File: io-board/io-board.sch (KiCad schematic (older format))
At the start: 11 parts, among them J1 EXP, J2 EXP, J3 Conn_01x12, J5 Conn_01x06, U1 W65C22N, U2 74HC138, U3 W65C51N, X1 1.8432MHz

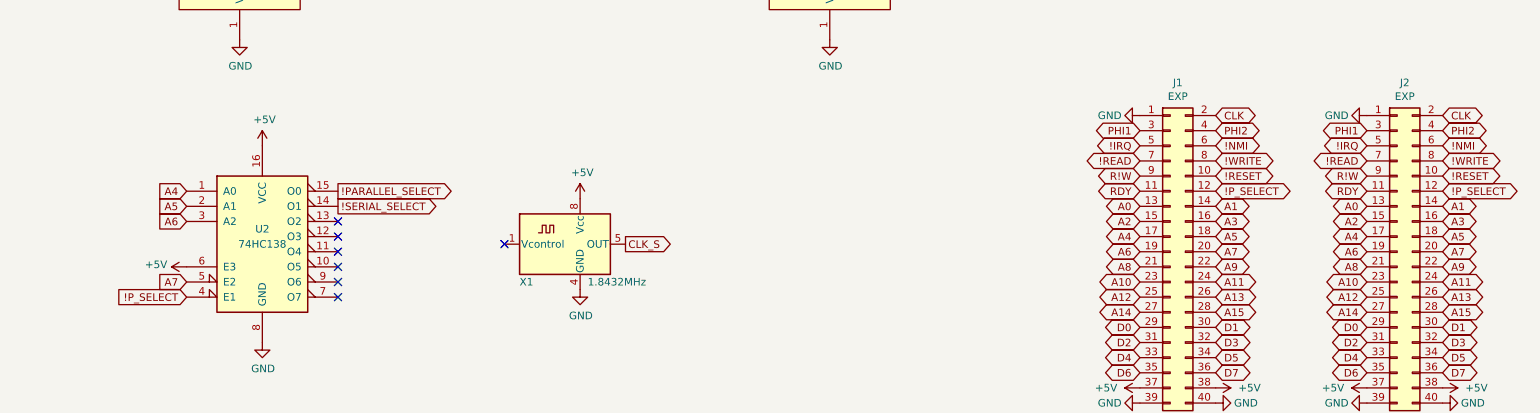
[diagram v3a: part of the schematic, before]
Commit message: remove old peripheral boards, begn new vga design
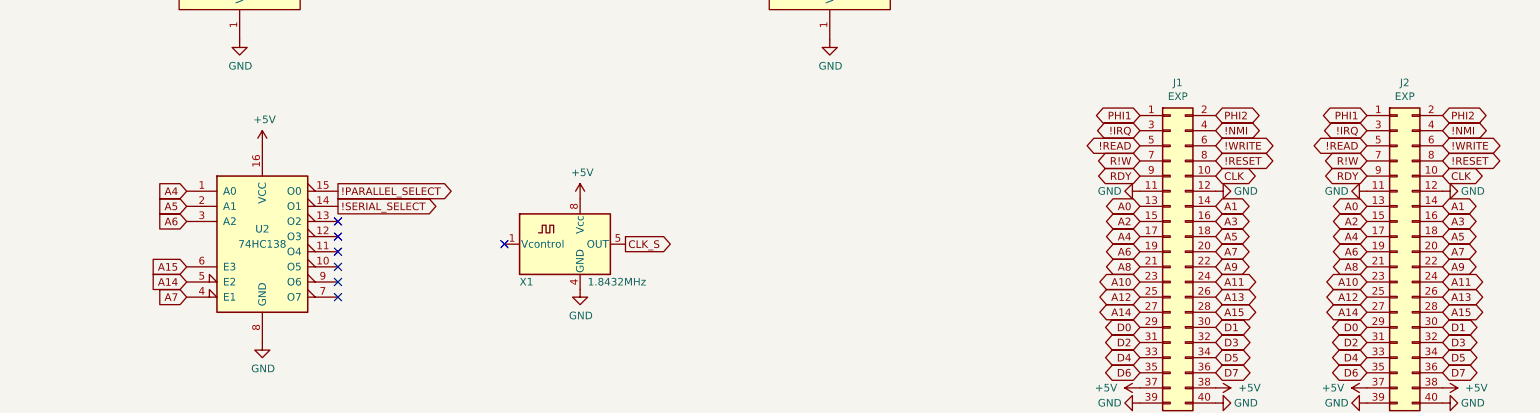
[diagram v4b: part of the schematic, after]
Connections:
- net !IRQ: now also J1.3 (Pin_3), J2.3 (Pin_3); no longer J1.5 (Pin_5), J2.5 (Pin_5)
- net !NMI: now also J1.4 (Pin_4), J2.4 (Pin_4); no longer J1.6 (Pin_6), J2.6 (Pin_6)
- net !READ: now also J1.5 (Pin_5), J2.5 (Pin_5); no longer J1.7 (Pin_7), J2.7 (Pin_7)
- net !RESET: now also J1.8 (Pin_8), J2.8 (Pin_8); no longer J1.10 (Pin_10), J2.10 (Pin_10)
- net !WRITE: now also J1.6 (Pin_6), J2.6 (Pin_6); no longer J1.8 (Pin_8), J2.8 (Pin_8)
- net +5V: no longer U2.6 (E3)
- net A14: now also U2.5 (E2)
- net A15: now also U2.6 (E3)
- net A7: now also U2.4 (E1); no longer U2.5 (E2)
- net CLK: now also J1.10 (Pin_10), J2.10 (Pin_10); no longer J1.2 (Pin_2), J2.2 (Pin_2)
- net GND: now also J1.11 (Pin_11), J1.12 (Pin_12), J2.11 (Pin_11), J2.12 (Pin_12); no longer J1.1 (Pin_1), J2.1 (Pin_1)
- net PHI1: now also J1.1 (Pin_1), J2.1 (Pin_1); no longer J1.3 (Pin_3), J2.3 (Pin_3)
- net PHI2: now also J1.2 (Pin_2), J2.2 (Pin_2); no longer J1.4 (Pin_4), J2.4 (Pin_4)
- net R!W: now also J1.7 (Pin_7), J2.7 (Pin_7); no longer J1.9 (Pin_9), J2.9 (Pin_9)
- net RDY: now also J1.9 (Pin_9), J2.9 (Pin_9); no longer J1.11 (Pin_11), J2.11 (Pin_11)
- removed net !P_SELECT: J1.12 (Pin_12), J2.12 (Pin_12), U2.4 (E1)
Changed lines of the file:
@@
 Text GLabel 7850 5950 0    50   BiDi ~ 0
 D6
+Text GLabel 7850 4250 0    50   BiDi ~ 0
+PHI1
+Text GLabel 8350 4250 2    50   BiDi ~ 0
+PHI2
+Text GLabel 8350 4550 2    50   BiDi ~ 0
+!RESET
 Text GLabel 7850 4350 0    50   BiDi ~ 0
-PHI1
+!IRQ
+Text GLabel 7850 4550 0    50   BiDi ~ 0
+R!W
+Text GLabel 7850 4650 0    50   BiDi ~ 0
+RDY
+Text GLabel 8350 4450 2    50   BiDi ~ 0
+!WRITE
+Text GLabel 7850 4450 0    50   BiDi ~ 0
+!READ
+Text GLabel 8350 4650 2    50   BiDi ~ 0
+CLK
 Text GLabel 8350 4350 2    50   BiDi ~ 0
-PHI2
-Text GLabel 8350 4650 2    50   BiDi ~ 0
-!RESET
-Text GLabel 7850 4450 0    50   BiDi ~ 0
-!IRQ
-Text GLabel 7850 4650 0    50   BiDi ~ 0
-R!W
-Text GLabel 7850 4750 0    50   BiDi ~ 0
-RDY
-Text GLabel 8350 4550 2    50   BiDi ~ 0
-!WRITE
-Text GLabel 7850 4550 0    50   BiDi ~ 0
-!READ
-Text GLabel 8350 4250 2    50   BiDi ~ 0
-CLK
-Text GLabel 8350 4450 2    50   BiDi ~ 0
 !NMI
 $Comp
@@
 L power:GND #PWR0107
 U 1 1 5FCC8CC9
-P 7850 4250
-F 0 "#PWR0107" H 7850 4000 50  0001 C CNN
-F 1 "GND" V 7850 4050 50  0000 C CNN
-F 2 "" H 7850 4250 50  0001 C CNN
-F 3 "" H 7850 4250 50  0001 C CNN
-	1    7850 4250
+P 7850 4750
+F 0 "#PWR0107" H 7850 4500 50  0001 C CNN
+F 1 "GND" V 7850 4550 50  0000 C CNN
+F 2 "" H 7850 4750 50  0001 C CNN
+F 3 "" H 7850 4750 50  0001 C CNN
+	1    7850 4750
 	0    1    1    0
 $EndComp
-Text GLabel 8350 4750 2    50   BiDi ~ 0
-!P_SELECT
+Text GLabel 9350 4250 0    50   BiDi ~ 0
+PHI1
 Text GLabel 9350 4350 0    50   BiDi ~ 0
-PHI1
+!IRQ
+Text GLabel 9350 4550 0    50   BiDi ~ 0
+R!W
+Text GLabel 9350 4650 0    50   BiDi ~ 0
+RDY
 Text GLabel 9350 4450 0    50   BiDi ~ 0
-!IRQ
-Text GLabel 9350 4650 0    50   BiDi ~ 0
-R!W
-Text GLabel 9350 4750 0    50   BiDi ~ 0
-RDY
-Text GLabel 9350 4550 0    50   BiDi ~ 0
 !READ
 $Comp
 L power:GND #PWR0111
 U 1 1 5FCCC288
-P 9350 4250
-F 0 "#PWR0111" H 9350 4000 50  0001 C CNN
-F 1 "GND" V 9350 4050 50  0000 C CNN
-F 2 "" H 9350 4250 50  0001 C CNN
-F 3 "" H 9350 4250 50  0001 C CNN
-	1    9350 4250
+P 9350 4750
+F 0 "#PWR0111" H 9350 4500 50  0001 C CNN
+F 1 "GND" V 9350 4550 50  0000 C CNN
+F 2 "" H 9350 4750 50  0001 C CNN
+F 3 "" H 9350 4750 50  0001 C CNN
+	1    9350 4750
 	0    1    1    0
 $EndComp
+Text GLabel 9850 4250 2    50   BiDi ~ 0
+PHI2
+Text GLabel 9850 4550 2    50   BiDi ~ 0
+!RESET
+Text GLabel 9850 4450 2    50   BiDi ~ 0
+!WRITE
+Text GLabel 9850 4650 2    50   BiDi ~ 0
+CLK
 Text GLabel 9850 4350 2    50   BiDi ~ 0
-PHI2
-Text GLabel 9850 4650 2    50   BiDi ~ 0
-!RESET
-Text GLabel 9850 4550 2    50   BiDi ~ 0
-!WRITE
-Text GLabel 9850 4250 2    50   BiDi ~ 0
-CLK
-Text GLabel 9850 4450 2    50   BiDi ~ 0
 !NMI
-Text GLabel 9850 4750 2    50   BiDi ~ 0
-!P_SELECT
-$Comp
-L power:+5V #PWR0112
-U 1 1 5FCCF7A4
-P 1550 5250
-F 0 "#PWR0112" H 1550 5100 50  0001 C CNN
-F 1 "+5V" V 1565 5378 50  0000 L CNN
-F 2 "" H 1550 5250 50  0001 C CNN
-F 3 "" H 1550 5250 50  0001 C CNN
-	1    1550 5250
-	0    -1   -1   0
-$EndComp
 Text GLabel 1550 5450 0    50   Input ~ 0
-!P_SELECT
+A7
+$Comp
+L power:GND #PWR?
+U 1 1 5FF86D9A
+P 8350 4750
+F 0 "#PWR?" H 8350 4500 50  0001 C CNN
+F 1 "GND" V 8350 4550 50  0000 C CNN
+F 2 "" H 8350 4750 50  0001 C CNN
+F 3 "" H 8350 4750 50  0001 C CNN
+	1    8350 4750
+	0    -1   -1   0
+$EndComp
+$Comp
+L power:GND #PWR?
+U 1 1 5FF9509A
+P 9850 4750
+F 0 "#PWR?" H 9850 4500 50  0001 C CNN
+F 1 "GND" V 9850 4550 50  0000 C CNN
+F 2 "" H 9850 4750 50  0001 C CNN
+F 3 "" H 9850 4750 50  0001 C CNN
+	1    9850 4750
+	0    -1   -1   0
+$EndComp
+Text GLabel 1550 5250 0    50   Input ~ 0
+A15
 Text GLabel 1550 5350 0    50   Input ~ 0
-A7
+A14
 $EndSCHEMATC
